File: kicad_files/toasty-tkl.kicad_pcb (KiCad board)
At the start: 2 copper layers, 345.7 x 134.1 mm, 204 parts, among them CON1 USB-MINI-B, Q1 60V 1.2A, SW0:0 ESC, SW0:10 F9, SW0:11 F10, SW0:12 F11, SW0:13 F12, SW0:14 PRINT, SW0:15 SCROLL LOCK, SW0:2 F1, SW0:3 F2, SW0:4 F3, SW0:5 F4, SW0:6 F5, SW0:7 F6, SW0:8 F7, SW0:9 F8, SW1:0 `, SW1:1 1, SW1:10 0, SW1:11 -, SW1:12 =, SW1:13 BACK SPACE, SW1:14 INSERT, SW1:15 HOME, SW1:2 2, SW1:3 3, SW1:4 4, SW1:5 5, SW1:6 6, SW1:7 7, SW1:8 8, SW1:9 9, SW2:0 TAB, SW2:1 Q, SW2:10 P, SW2:11 [, SW2:12 ], SW2:13 \, SW2:14 DELETE, SW2:15 END, SW2:2 W, SW2:3 E, SW2:4 R, SW2:5 T, SW2:6 Y, SW2:7 U, SW2:8 I, SW2:9 O, SW3:0 CAPS LOCK, SW3:1 A, SW3:10 ;, SW3:11 ', SW3:13 ENTER, SW3:14 PAGE UP, SW3:15 PAUSE, SW3:2 S, SW3:3 D, SW3:4 F, SW3:5 G, SW3:6 H, SW3:7 J, SW3:8 K, SW3:9 L, SW4:0 LEFT SHIFT, SW4:1 Z, SW4:10 /, SW4:13 RIGHT SHIFT, SW4:14 PAGE DOWN, SW4:15 UP, SW4:2 X, SW4:3 C, SW4:4 V, SW4:5 B, SW4:6 N, SW4:7 M, SW4:8 ,, SW4:9 ., SW5:0 LEFT CTRL, SW5:1 LEFT WINDOWS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

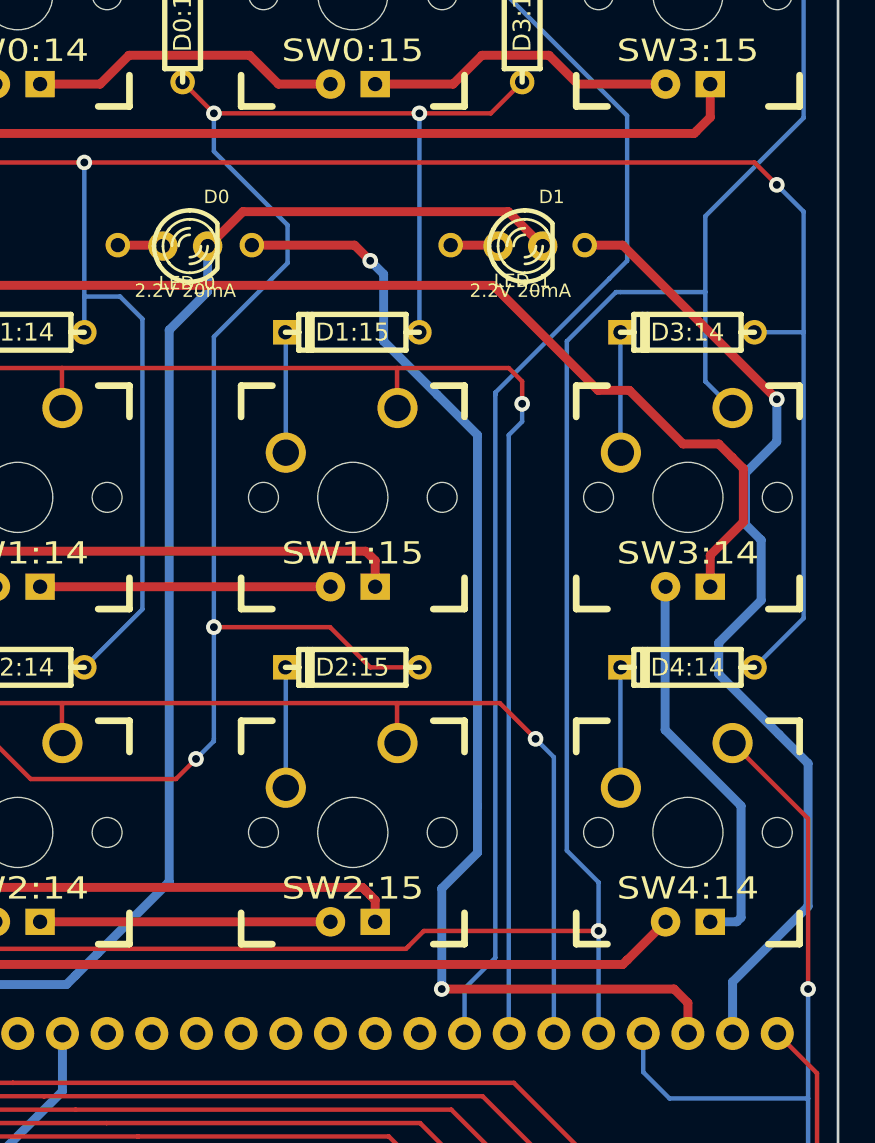
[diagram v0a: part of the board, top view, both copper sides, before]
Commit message: Adjusted module positions.  Increased silk screen font size.
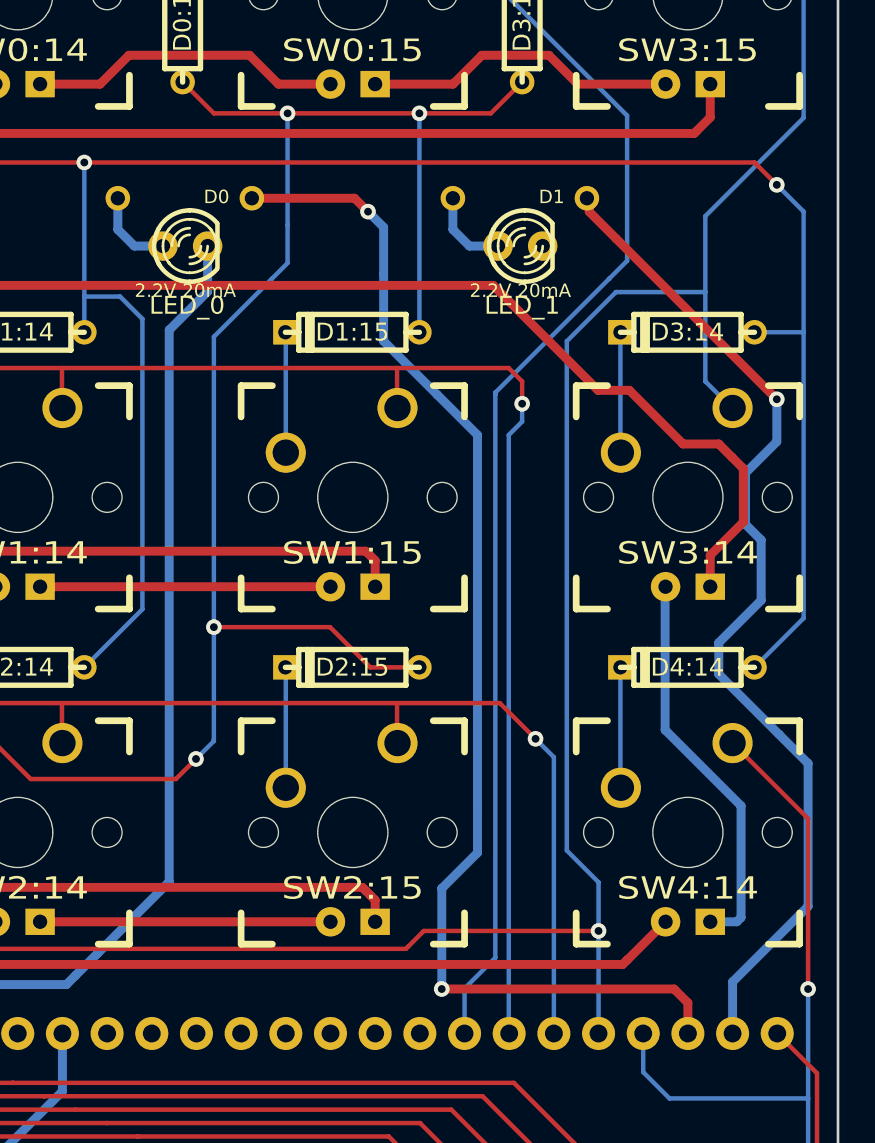
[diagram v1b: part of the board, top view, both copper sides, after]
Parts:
- moved LED_R1 2.67 mm to (346.1, 37.8)
- moved LED_R0 2.67 mm to (327.0, 37.8)
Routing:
- net /GND: track 197.6 -> 177.0 mm
- net /LED 0: track 67.9 -> 70.6 mm
- net N-0000099: track 2.59 -> 4.73 mm
- net N-0000098: track 2.71 -> 4.73 mm
- net /COL 15: track 222.3 -> 220.5 mm
- net /LED 1: track 56.6 -> 57.9 mm

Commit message: Removed unnecessary vias, cleaned up GND
Removed 3 vias from the boost converter area
Removed an extra branch from a ground line running through the Teensy's
Pin 1
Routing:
- net /GND: track 177.0 -> 179.1 mm, vias 4 -> 3
- net N-00000117: track 76.6 -> 75.5 mm, vias 2 -> 1
- net N-00000173: track 300.6 -> 300.4 mm, vias 6 -> 5

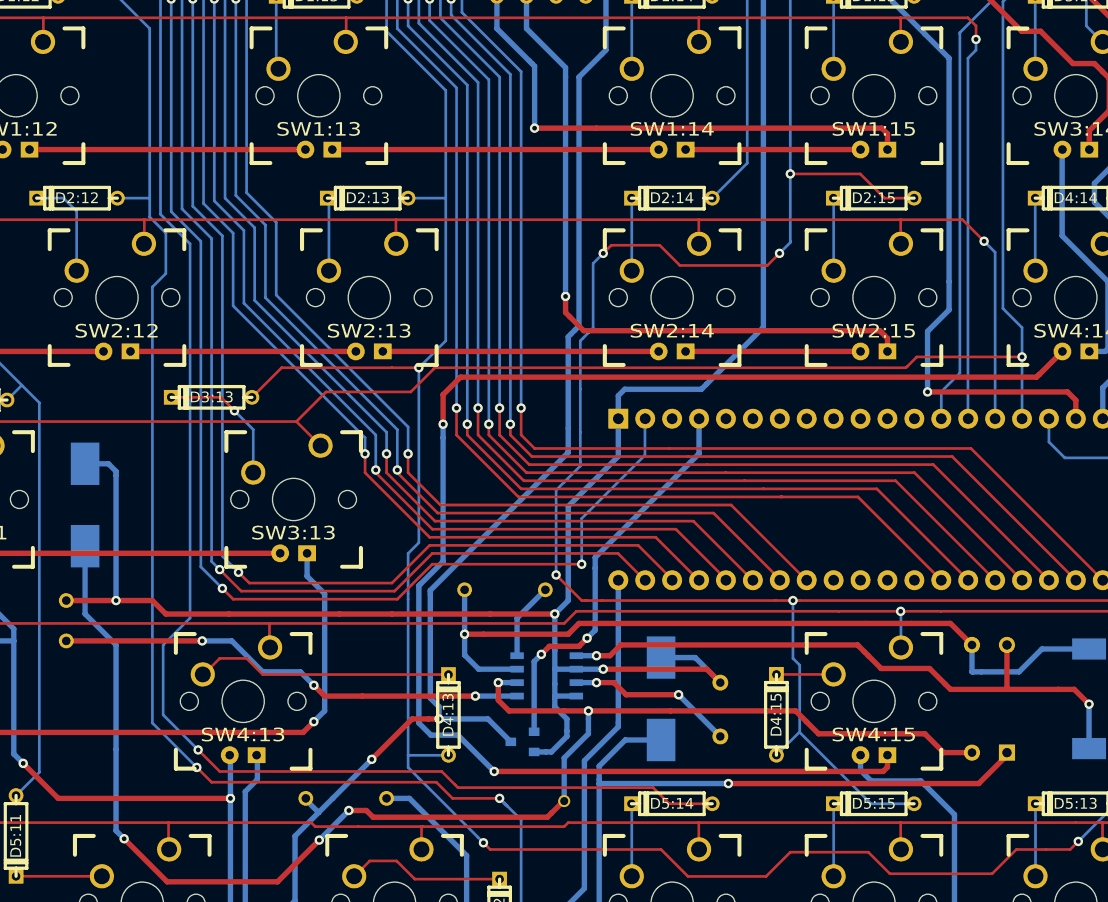
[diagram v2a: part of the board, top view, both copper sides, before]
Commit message: Cleaned up files, made notes folder, removed old notes.  Modified a few traces.  Added logo and sig.
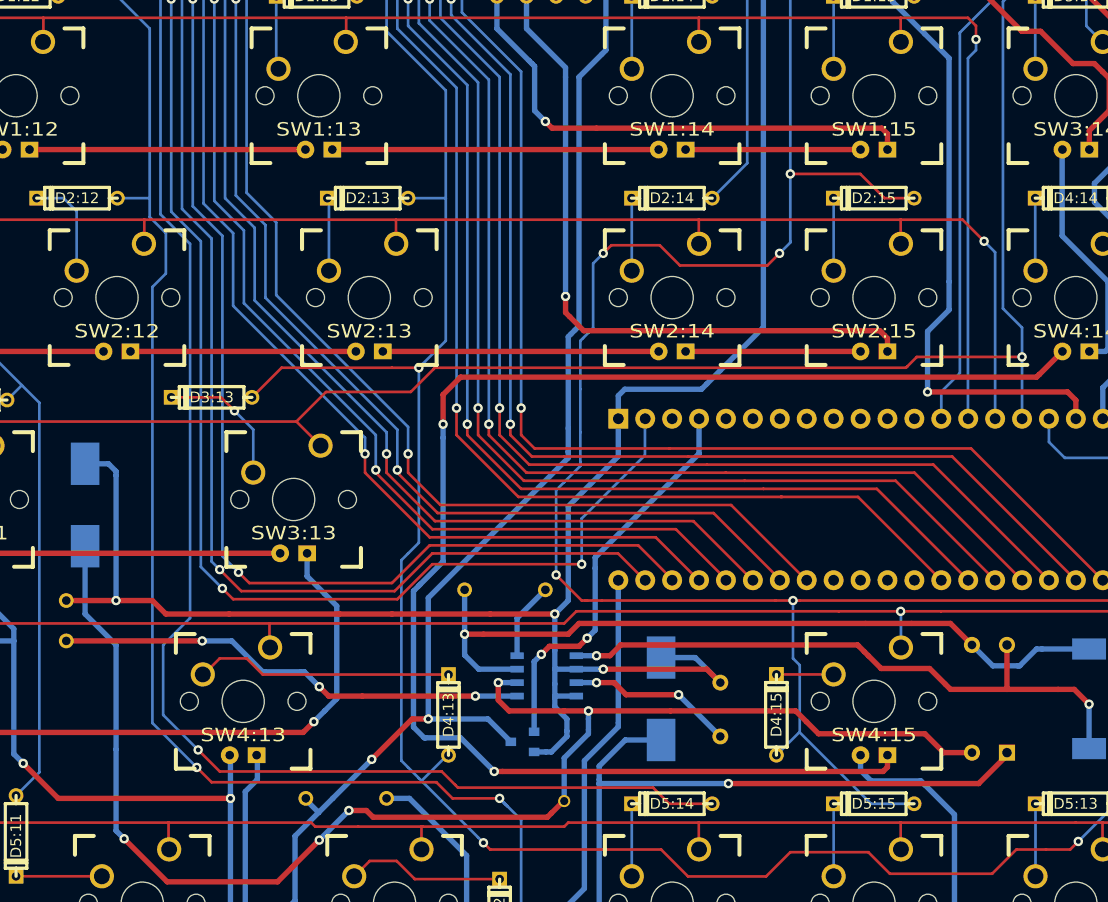
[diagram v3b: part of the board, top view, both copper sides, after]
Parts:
- added G***: OC_LOGO, OC_LOGO, B.Cu at (112.6, 130.2)
- added G***: TOAST_LOGO, TOAST_LOGO, B.Cu at (45.7, 26.8)
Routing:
- net N-00000117: track 75.5 -> 73.6 mm
- net /LEDROW6: track 49.0 -> 48.0 mm
- net N-00000113: track 101.0 -> 101.9 mm
- net N-0000093: track 139.5 -> 140.4 mm
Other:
- board text removed: "ToastyTKL"
- board text removed: "rev 1"
